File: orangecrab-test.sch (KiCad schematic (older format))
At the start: 27 parts, among them J1 Conn_01x16, J2 Conn_01x12, SW1 SW_Push, U1 DAC53608RTET, U2 MCP23S08T-E-ML

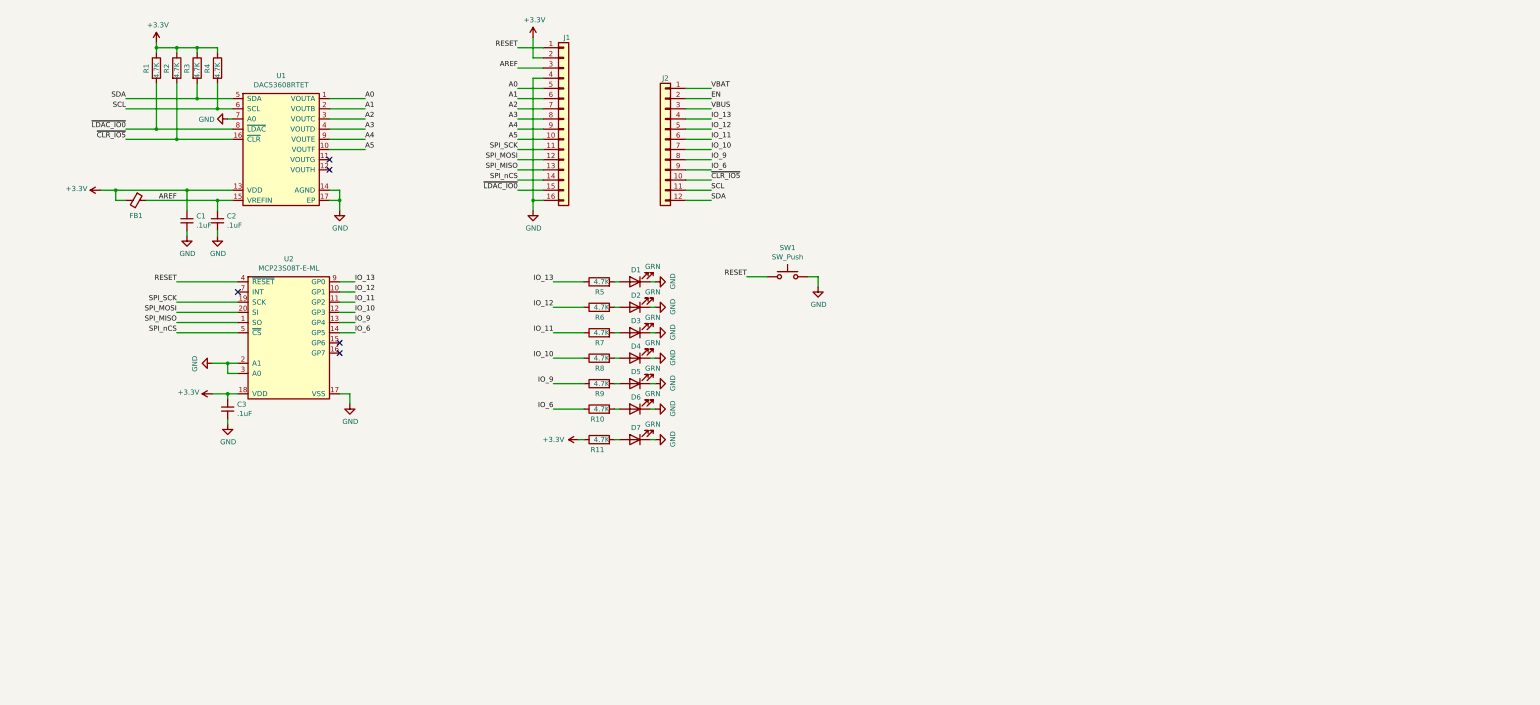
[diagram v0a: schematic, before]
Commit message: Add FTDI from programming the initial firmware
Signed-off-by: Michael Welling <mwelling@ieee.org>
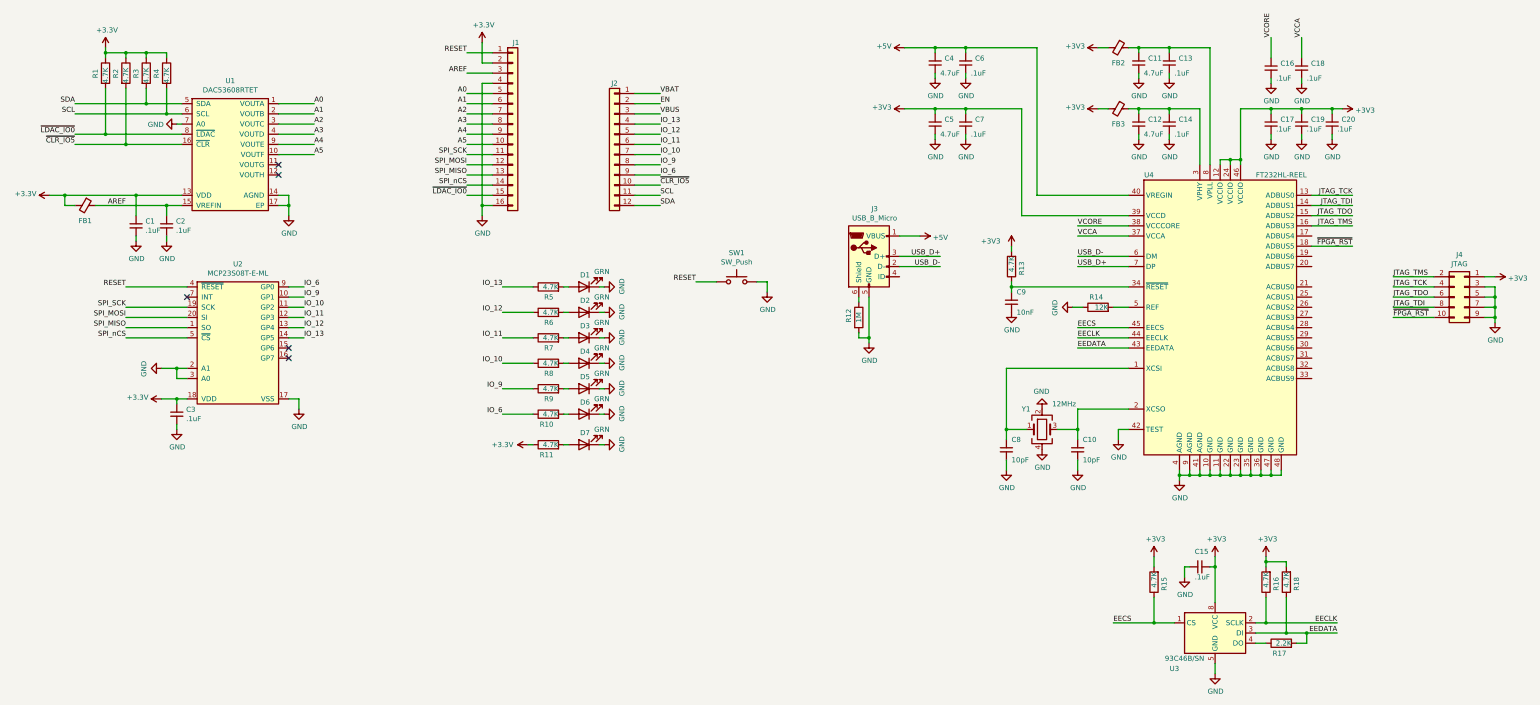
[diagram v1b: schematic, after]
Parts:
- added C10, C8: 10pF, Capacitor_SMD:C_0402_1005Metric, symbol Device:C_Small
- added C11, C12: 4.7uF, Capacitor_SMD:C_0603_1608Metric, symbol Device:C_Small
- added C13, C14, C15, C16, C17, C18, C19, C20, C6, C7: .1uF, Capacitor_SMD:C_0402_1005Metric, symbol Device:C_Small
- added C4, C5: 4.7uF, Capacitor_SMD:C_0402_1005Metric, symbol Device:C_Small
- added C9: 10nF, Capacitor_SMD:C_0402_1005Metric, symbol Device:C_Small
- added FB2, FB3: Ferrite_Bead_Small, Inductor_SMD:L_0603_1608Metric, symbol Device:Ferrite_Bead_Small
- added J3: USB_B_Micro, Connector_USB:USB_Micro-B_Molex-105017-0001, symbol Connector:USB_B_Micro
- added J4: JTAG, Connector_PinHeader_1.27mm:PinHeader_2x05_P1.27mm_Vertical_SMD, symbol Connector_Generic:Conn_02x05_Odd_Even
- added R12: 1M, Resistor_SMD:R_0402_1005Metric, symbol Device:R
- added R13, R15, R16, R18: 4.7K, Resistor_SMD:R_0402_1005Metric, symbol Device:R
- added R14: 12K, Resistor_SMD:R_0402_1005Metric, symbol Device:R
- added R17: 2.2K, Resistor_SMD:R_0402_1005Metric, symbol Device:R
- added U3: 93C46B/SN, Package_SO:SOIC-8_3.9x4.9mm_P1.27mm, symbol Memory_EEPROM:93CxxB
- added U4: FT232HL-REEL, Package_QFP:TQFP-48-1EP_7x7mm_P0.5mm_EP5x5mm, symbol Interface_USB:FT232H
- added Y1: 12MHz, Crystal:Crystal_SMD_2520-4Pin_2.5x2.0mm, symbol Device:Crystal_GND24
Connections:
- net +3V3: now also C15.1, C17.1, C19.1, C20.1, C5.1, C7.1, FB2.2, FB3.2, J4.1 (Pin_1), R13.2, R15.2, R16.2, R18.2, U3.8 (VCC), U4.12 (VCCIO), U4.24 (VCCIO), U4.39 (VCCD), U4.46 (VCCIO)
- net GND: now also C10.2, C11.2, C12.2, C13.2, C14.2, C15.2, C16.2, C17.2, C18.2, C19.2, C20.2, C4.2, C5.2, C6.2, C7.2, C8.2, C9.2, J3.5 (GND), J4.3 (Pin_3), J4.5 (Pin_5), J4.7 (Pin_7), J4.9 (Pin_9), R12.2, R14.1, U3.5 (GND), U4.10 (GND), U4.11 (GND), U4.22 (GND), U4.23 (GND), U4.35 (GND), U4.36 (GND), U4.4 (AGND), U4.41 (AGND), U4.42 (TEST), U4.47 (GND), U4.48 (GND), U4.9 (AGND), Y1.2, Y1.4
- net IO_10: now also U2.11 (GP2); no longer U2.12 (GP3)
- net IO_11: now also U2.12 (GP3); no longer U2.11 (GP2)
- net IO_12: now also U2.13 (GP4); no longer U2.10 (GP1)
- net IO_13: now also U2.14 (GP5); no longer U2.9 (GP0)
- net IO_6: now also U2.9 (GP0); no longer U2.14 (GP5)
- net IO_9: now also U2.10 (GP1); no longer U2.13 (GP4)
- new net: C8.1, U4.1 (XCSI), Y1.1
- new net: C10.1, U4.2 (XCSO), Y1.3
- new net: C12.1, C14.1, FB3.1, U4.3 (VPHY)
- new net: C9.1, R13.1, U4.34 (~RESET)
- new net: R14.2, U4.5 (REF)
- new net: C11.1, C13.1, FB2.1, U4.8 (VPLL)
- new net: R17.1, U3.4 (DO)
- new net: J3.6 (Shield), R12.1
- new net +5V: C4.1, C6.1, J3.1 (VBUS), U4.40 (VREGIN)
- new net EECLK: R16.1, U3.2 (SCLK), U4.44 (EECLK)
- new net EECS: R15.1, U3.1 (CS), U4.45 (EECS)
- new net EEDATA: R17.2, R18.1, U3.3 (DI), U4.43 (EEDATA)
- new net JTAG_TCK: J4.4 (Pin_4), U4.13 (ADBUS0)
- new net JTAG_TDI: J4.8 (Pin_8), U4.14 (ADBUS1)
- new net JTAG_TDO: J4.6 (Pin_6), U4.15 (ADBUS2)
- new net JTAG_TMS: J4.2 (Pin_2), U4.16 (ADBUS3)
- new net USB_D+: J3.3 (D+), U4.7 (DP)
- new net USB_D-: J3.2 (D-), U4.6 (DM)
- new net VCCA: C18.1, U4.37 (VCCA)
- new net VCORE: C16.1, U4.38 (VCCCORE)
- new net ~FPGA_RST: J4.10 (Pin_10), U4.18 (ADBUS5)
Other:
- moved on the sheet: C1, C2, C3, D1, D2, D3, D4, D5, D6, D7, FB1, J1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

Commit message: Route board
Consider making the FTDI a snap off section.

Signed-off-by: Michael Welling <mwelling@ieee.org>
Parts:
- added H1, H2, H3, H4: MountingHole, MountingHole:MountingHole_3.5mm, symbol Mechanical:MountingHole
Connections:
- net +3V3: no longer C15.1, C17.1, C19.1, C20.1, C5.1, C7.1, FB2.2, FB3.2, J4.1 (Pin_1), R13.2, R15.2, R16.2, R18.2, U3.8 (VCC), U4.12 (VCCIO), U4.24 (VCCIO), U4.39 (VCCD), U4.46 (VCCIO)
- new net: C15.1, U3.8 (VCC)
- new net +3.3VA: C17.1, C19.1, C20.1, C5.1, C7.1, FB2.2, FB3.2, R13.2, R15.2, R16.2, R18.2, U4.12 (VCCIO), U4.24 (VCCIO), U4.39 (VCCD), U4.46 (VCCIO)
- no-connect marks 5 -> 6
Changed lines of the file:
@@
 	11400 4150 11500 4150
-$Comp
-L power:+3V3 #PWR0132
-U 1 1 5EC7E2DC
-P 10800 3550
-F 0 "#PWR0132" H 10800 3400 50  0001 C CNN
-F 1 "+3V3" H 10500 3600 50  0000 L CNN
-F 2 "" H 10800 3550 50  0001 C CNN
-F 3 "" H 10800 3550 50  0001 C CNN
-	1    10800 3550
-	1    0    0    -1
-$EndComp
 $Comp
 L Device:R R13
@@
 	13050 2200 13050 2700
 Connection ~ 13050 2700
-$Comp
-L power:+3V3 #PWR0140
-U 1 1 5ED4604E
-P 11650 1600
-F 0 "#PWR0140" H 11650 1450 50  0001 C CNN
-F 1 "+3V3" V 11665 1728 50  0000 L CNN
-F 2 "" H 11650 1600 50  0001 C CNN
-F 3 "" H 11650 1600 50  0001 C CNN
-	1    11650 1600
-	0    -1   -1   0
-$EndComp
-$Comp
-L power:+3V3 #PWR0141
-U 1 1 5ED462A2
-P 11650 2200
-F 0 "#PWR0141" H 11650 2050 50  0001 C CNN
-F 1 "+3V3" V 11665 2328 50  0000 L CNN
-F 2 "" H 11650 2200 50  0001 C CNN
-F 3 "" H 11650 2200 50  0001 C CNN
-	1    11650 2200
-	0    -1   -1   0
-$EndComp
 Wire Wire Line
 	11650 1600 11750 1600
 Wire Wire Line
 	11650 2200 11750 2200
-$Comp
-L power:+3V3 #PWR0142
-U 1 1 5ED5C01E
-P 14050 2200
-F 0 "#PWR0142" H 14050 2050 50  0001 C CNN
-F 1 "+3V3" V 14065 2328 50  0000 L CNN
-F 2 "" H 14050 2200 50  0001 C CNN
-F 3 "" H 14050 2200 50  0001 C CNN
-	1    14050 2200
-	0    1    1    0
-$EndComp
 Wire Wire Line
 	13950 2200 14050 2200
@@
 Wire Wire Line
 	10350 2200 10050 2200
-$Comp
-L power:+3V3 #PWR0148
-U 1 1 5EDF2C7E
-P 9750 2200
-F 0 "#PWR0148" H 9750 2050 50  0001 C CNN
-F 1 "+3V3" V 9765 2328 50  0000 L CNN
-F 2 "" H 9750 2200 50  0001 C CNN
-F 3 "" H 9750 2200 50  0001 C CNN
-	1    9750 2200
-	0    -1   -1   0
-$EndComp
 Wire Wire Line
 	9750 2200 10050 2200
@@
 Wire Wire Line
 	12800 6700 12750 6700
-$Comp
-L power:+3V3 #PWR0153
-U 1 1 5EF89E05
-P 12800 6600
-F 0 "#PWR0153" H 12800 6450 50  0001 C CNN
-F 1 "+3V3" H 12815 6773 50  0000 C CNN
-F 2 "" H 12800 6600 50  0001 C CNN
-F 3 "" H 12800 6600 50  0001 C CNN
-	1    12800 6600
-	1    0    0    -1
-$EndComp
 Wire Wire Line
 	12800 6700 12800 6600
@@
 $EndComp
 $Comp
-L power:+3V3 #PWR0154
-U 1 1 5F163EF8
-P 15550 3850
-F 0 "#PWR0154" H 15550 3700 50  0001 C CNN
-F 1 "+3V3" V 15565 3978 50  0000 L CNN
-F 2 "" H 15550 3850 50  0001 C CNN
-F 3 "" H 15550 3850 50  0001 C CNN
-	1    15550 3850
-	0    1    1    0
-$EndComp
-Wire Wire Line
-	15450 3850 15550 3850
-$Comp
 L power:GND #PWR0155
 U 1 1 5F173112
@@
 Wire Wire Line
 	13500 7350 13700 7350
-$Comp
-L power:+3V3 #PWR0156
-U 1 1 5F1D01BE
-P 13300 6600
-F 0 "#PWR0156" H 13300 6450 50  0001 C CNN
-F 1 "+3V3" H 13315 6773 50  0000 C CNN
-F 2 "" H 13300 6600 50  0001 C CNN
-F 3 "" H 13300 6600 50  0001 C CNN
-	1    13300 6600
-	1    0    0    -1
-$EndComp
 Wire Wire Line
 	13300 6700 13300 6650
@@
 Wire Wire Line
 	12200 7000 12200 7250
-$Comp
-L power:+3V3 #PWR0157
-U 1 1 5F22302D
-P 12200 6600
-F 0 "#PWR0157" H 12200 6450 50  0001 C CNN
-F 1 "+3V3" H 12215 6773 50  0000 C CNN
-F 2 "" H 12200 6600 50  0001 C CNN
-F 3 "" H 12200 6600 50  0001 C CNN
-	1    12200 6600
-	1    0    0    -1
-$EndComp
 Wire Wire Line
 	12800 6700 12800 7050
-Wire Wire Line
-	12200 6700 12200 6600
 Connection ~ 12200 7250
 Wire Wire Line
@@
 Text Label 14150 3550 2    50   ~ 0
 ~FPGA_RST
+$Comp
+L Mechanical:MountingHole H4
+U 1 1 5EB87D65
+P 13450 8900
+F 0 "H4" H 13550 8946 50  0000 L CNN
+F 1 "MountingHole" H 13550 8855 50  0000 L CNN
+F 2 "MountingHole:MountingHole_3.5mm" H 13450 8900 50  0001 C CNN
+F 3 "~" H 13450 8900 50  0001 C CNN
+	1    13450 8900
+	1    0    0    -1
+$EndComp
+$Comp
+L Mechanical:MountingHole H3
+U 1 1 5EB88028
+P 13450 8650
+F 0 "H3" H 13550 8696 50  0000 L CNN
+F 1 "MountingHole" H 13550 8605 50  0000 L CNN
+F 2 "MountingHole:MountingHole_3.5mm" H 13450 8650 50  0001 C CNN
+F 3 "~" H 13450 8650 50  0001 C CNN
+	1    13450 8650
+	1    0    0    -1
+$EndComp
+$Comp
+L Mechanical:MountingHole H2
+U 1 1 5EB99EEE
+P 13450 8400
+F 0 "H2" H 13550 8446 50  0000 L CNN
+F 1 "MountingHole" H 13550 8355 50  0000 L CNN
+F 2 "MountingHole:MountingHole_3.5mm" H 13450 8400 50  0001 C CNN
+F 3 "~" H 13450 8400 50  0001 C CNN
+	1    13450 8400
+	1    0    0    -1
+$EndComp
+$Comp
+L Mechanical:MountingHole H1
+U 1 1 5EBABDBC
+P 13450 8150
+F 0 "H1" H 13550 8196 50  0000 L CNN
+F 1 "MountingHole" H 13550 8105 50  0000 L CNN
+F 2 "MountingHole:MountingHole_3.5mm" H 13450 8150 50  0001 C CNN
+F 3 "~" H 13450 8150 50  0001 C CNN
+	1    13450 8150
+	1    0    0    -1
+$EndComp
+NoConn ~ 15450 3850
+$Comp
+L power:+3.3VA #PWR?
+U 1 1 5EBD0DE3
+P 9750 2200
+F 0 "#PWR?" H 9750 2050 50  0001 C CNN
+F 1 "+3.3VA" V 9765 2327 50  0000 L CNN
+F 2 "" H 9750 2200 50  0001 C CNN
+F 3 "" H 9750 2200 50  0001 C CNN
+	1    9750 2200
+	0    -1   -1   0
+$EndComp
+$Comp
+L power:+3.3VA #PWR?
+U 1 1 5EBD16BF
+P 11650 1600
+F 0 "#PWR?" H 11650 1450 50  0001 C CNN
+F 1 "+3.3VA" V 11665 1727 50  0000 L CNN
+F 2 "" H 11650 1600 50  0001 C CNN
+F 3 "" H 11650 1600 50  0001 C CNN
+	1    11650 1600
+	0    -1   -1   0
+$EndComp
+$Comp
+L power:+3.3VA #PWR?
+U 1 1 5EBD183E
+P 11650 2200
+F 0 "#PWR?" H 11650 2050 50  0001 C CNN
+F 1 "+3.3VA" V 11665 2327 50  0000 L CNN
+F 2 "" H 11650 2200 50  0001 C CNN
+F 3 "" H 11650 2200 50  0001 C CNN
+	1    11650 2200
+	0    -1   -1   0
+$EndComp
+$Comp
+L power:+3.3VA #PWR?
+U 1 1 5EBD197F
+P 14050 2200
+F 0 "#PWR?" H 14050 2050 50  0001 C CNN
+F 1 "+3.3VA" V 14065 2328 50  0000 L CNN
+F 2 "" H 14050 2200 50  0001 C CNN
+F 3 "" H 14050 2200 50  0001 C CNN
+	1    14050 2200
+	0    1    1    0
+$EndComp
+$Comp
+L power:+3.3VA #PWR?
+U 1 1 5EBD1A82
+P 10800 3550
+F 0 "#PWR?" H 10800 3400 50  0001 C CNN
+F 1 "+3.3VA" H 10815 3723 50  0000 C CNN
+F 2 "" H 10800 3550 50  0001 C CNN
+F 3 "" H 10800 3550 50  0001 C CNN
+	1    10800 3550
+	1    0    0    -1
+$EndComp
+$Comp
+L power:+3.3VA #PWR?
+U 1 1 5EBD1C7D
+P 12200 6600
+F 0 "#PWR?" H 12200 6450 50  0001 C CNN
+F 1 "+3.3VA" H 12215 6773 50  0000 C CNN
+F 2 "" H 12200 6600 50  0001 C CNN
+F 3 "" H 12200 6600 50  0001 C CNN
+	1    12200 6600
+	1    0    0    -1
+$EndComp
+Wire Wire Line
+	12200 6600 12200 6700
+$Comp
+L power:+3.3VA #PWR?
+U 1 1 5EBE3E73
+P 13300 6600
+F 0 "#PWR?" H 13300 6450 50  0001 C CNN
+F 1 "+3.3VA" H 13315 6773 50  0000 C CNN
+F 2 "" H 13300 6600 50  0001 C CNN
+F 3 "" H 13300 6600 50  0001 C CNN
+	1    13300 6600
+	1    0    0    -1
+$EndComp
 $EndSCHEMATC

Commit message: Add a few more mounting holes
Signed-off-by: Michael Welling <mwelling@ieee.org>
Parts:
- added H5, H6, H7, H8: MountingHole, MountingHole:MountingHole_3.5mm, symbol Mechanical:MountingHole
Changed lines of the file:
@@
 NoConn ~ 15450 3850
 $Comp
-L power:+3.3VA #PWR?
+L power:+3.3VA #PWR01
 U 1 1 5EBD0DE3
 P 9750 2200
-F 0 "#PWR?" H 9750 2050 50  0001 C CNN
+F 0 "#PWR01" H 9750 2050 50  0001 C CNN
 F 1 "+3.3VA" V 9765 2327 50  0000 L CNN
 F 2 "" H 9750 2200 50  0001 C CNN
@@
 $EndComp
 $Comp
-L power:+3.3VA #PWR?
+L power:+3.3VA #PWR03
 U 1 1 5EBD16BF
 P 11650 1600
-F 0 "#PWR?" H 11650 1450 50  0001 C CNN
+F 0 "#PWR03" H 11650 1450 50  0001 C CNN
 F 1 "+3.3VA" V 11665 1727 50  0000 L CNN
 F 2 "" H 11650 1600 50  0001 C CNN
@@
 $EndComp
 $Comp
-L power:+3.3VA #PWR?
+L power:+3.3VA #PWR04
 U 1 1 5EBD183E
 P 11650 2200
-F 0 "#PWR?" H 11650 2050 50  0001 C CNN
+F 0 "#PWR04" H 11650 2050 50  0001 C CNN
 F 1 "+3.3VA" V 11665 2327 50  0000 L CNN
 F 2 "" H 11650 2200 50  0001 C CNN
@@
 $EndComp
 $Comp
-L power:+3.3VA #PWR?
+L power:+3.3VA #PWR07
 U 1 1 5EBD197F
 P 14050 2200
-F 0 "#PWR?" H 14050 2050 50  0001 C CNN
+F 0 "#PWR07" H 14050 2050 50  0001 C CNN
 F 1 "+3.3VA" V 14065 2328 50  0000 L CNN
 F 2 "" H 14050 2200 50  0001 C CNN
@@
 $EndComp
 $Comp
-L power:+3.3VA #PWR?
+L power:+3.3VA #PWR02
 U 1 1 5EBD1A82
 P 10800 3550
-F 0 "#PWR?" H 10800 3400 50  0001 C CNN
+F 0 "#PWR02" H 10800 3400 50  0001 C CNN
 F 1 "+3.3VA" H 10815 3723 50  0000 C CNN
 F 2 "" H 10800 3550 50  0001 C CNN
@@
 $EndComp
 $Comp
-L power:+3.3VA #PWR?
+L power:+3.3VA #PWR05
 U 1 1 5EBD1C7D
 P 12200 6600
-F 0 "#PWR?" H 12200 6450 50  0001 C CNN
+F 0 "#PWR05" H 12200 6450 50  0001 C CNN
 F 1 "+3.3VA" H 12215 6773 50  0000 C CNN
 F 2 "" H 12200 6600 50  0001 C CNN
@@
 	12200 6600 12200 6700
 $Comp
-L power:+3.3VA #PWR?
+L power:+3.3VA #PWR06
 U 1 1 5EBE3E73
 P 13300 6600
-F 0 "#PWR?" H 13300 6450 50  0001 C CNN
+F 0 "#PWR06" H 13300 6450 50  0001 C CNN
 F 1 "+3.3VA" H 13315 6773 50  0000 C CNN
 F 2 "" H 13300 6600 50  0001 C CNN
@@
 	1    0    0    -1
 $EndComp
+$Comp
+L Mechanical:MountingHole H6
+U 1 1 5EB8A3E3
+P 14250 8400
+F 0 "H6" H 14350 8446 50  0000 L CNN
+F 1 "MountingHole" H 14350 8355 50  0000 L CNN
+F 2 "MountingHole:MountingHole_3.5mm" H 14250 8400 50  0001 C CNN
+F 3 "~" H 14250 8400 50  0001 C CNN
+	1    14250 8400
+	1    0    0    -1
+$EndComp
+$Comp
+L Mechanical:MountingHole H5
+U 1 1 5EB8A3EA
+P 14250 8150
+F 0 "H5" H 14350 8196 50  0000 L CNN
+F 1 "MountingHole" H 14350 8105 50  0000 L CNN
+F 2 "MountingHole:MountingHole_3.5mm" H 14250 8150 50  0001 C CNN
+F 3 "~" H 14250 8150 50  0001 C CNN
+	1    14250 8150
+	1    0    0    -1
+$EndComp
+$Comp
+L Mechanical:MountingHole H8
+U 1 1 5EBAE63F
+P 14250 8900
+F 0 "H8" H 14350 8946 50  0000 L CNN
+F 1 "MountingHole" H 14350 8855 50  0000 L CNN
+F 2 "MountingHole:MountingHole_3.5mm" H 14250 8900 50  0001 C CNN
+F 3 "~" H 14250 8900 50  0001 C CNN
+	1    14250 8900
+	1    0    0    -1
+$EndComp
+$Comp
+L Mechanical:MountingHole H7
+U 1 1 5EBAE646
+P 14250 8650
+F 0 "H7" H 14350 8696 50  0000 L CNN
+F 1 "MountingHole" H 14350 8605 50  0000 L CNN
+F 2 "MountingHole:MountingHole_3.5mm" H 14250 8650 50  0001 C CNN
+F 3 "~" H 14250 8650 50  0001 C CNN
+	1    14250 8650
+	1    0    0    -1
+$EndComp

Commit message: added 2 layers for board/pogo alignment. battery circuit
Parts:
- added C21, C23: 4.7uF, Capacitor_SMD:C_0402_1005Metric, symbol Device:C_Small
- added C22, C24, C?: .1uF, Capacitor_SMD:C_0402_1005Metric, symbol Device:C_Small
- added D8: PMEG3015EH,115, Diode_SMD:D_SOD-123F, symbol Device:D_ALT
- added Q1: DMG2302UK-7, Package_TO_SOT_SMD:SOT-23, symbol Device:Q_NMOS_GSD
- added R19: 402k, Resistor_SMD:R_0402_1005Metric, symbol Device:R
- added R20: 82R, Resistor_SMD:R_1206_3216Metric, symbol Device:R
- added R21: 169k, Resistor_SMD:R_0402_1005Metric, symbol Device:R
- added R22: 4.7K, Resistor_SMD:R_0402_1005Metric, symbol Device:R
- added U5: TPS76301DBVR, Package_TO_SOT_SMD:SOT-23-5, symbol Regulator_Linear:TPS76301
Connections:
- net +5V: now also C?.1, U5.1 (VIN)
- net GND: now also C21.2, C22.2, C23.2, C24.2, C?.2, Q1.2 (S), R21.2, R22.1, U5.2 (GND)
- net VBAT: now also C23.1, C24.1, D8.1 (K), R20.1
- net at U2.15 (GP6): now also U5.3 (EN)
- net at U2.16 (GP7): now also Q1.1 (G), R22.2
- new net: R19.2, R21.1, U5.4 (FB)
- new net: Q1.3 (D), R20.2
- new net 4V: C21.1, C22.1, D8.2 (A), R19.1, U5.5 (VOUT)
- no-connect marks 6 -> 4
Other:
- note added: "1. Test current around 3.3v \npresent across R\ntriggers battery charger"
- note added: "2. Charger passes 100-200mA \ncurrent through Resistor"
- note added: "3. NMOS is required to \n'disconnect' battery"

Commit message: Add regulator input pulldown and add silkscreen bling
Signed-off-by: Michael Welling <mwelling@ieee.org>
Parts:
- removed H7, H8: MountingHole, MountingHole:MountingHole_3.5mm, symbol Mechanical:MountingHole
- added R23: 4.7K, Resistor_SMD:R_0402_1005Metric, symbol Device:R
- gave numbers to parts that had none: 1
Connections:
- net GND: now also R23.1
- net at U2.15 (GP6), U5.3 (EN): now also R23.2
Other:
- moved on the sheet: C1, C2, C3, FB1, R1, R2, R3, R4, U1, U2

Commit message: Add BOM
Signed-off-by: Michael Welling <mwelling@ieee.org>
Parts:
- C1, C13, C14, C15, C16, C17, C18, C19, C2, C20, C22, C24, C25, C3, C6, C7: MPN (none) -> GRM155R71C104KA88J
- C10, C8: MPN (none) -> GRM1555C1H100JA01D
- C11, C12: MPN (none) -> C0603C475K9PACTU
- C21, C23, C4, C5: MPN (none) -> GRM155R60J475ME47D
- C9: MPN (none) -> C0402C103K4RECAUTO
- D1, D2, D3, D4, D5, D6, D7: MPN (none) -> LTST-C191GKT
- D8: MPN (none) -> PMEG3015EH,115
- FB1, FB2, FB3: MPN (none) -> 742792651
- H1, H2, H3, H4, H5, H6, J1, J2: MPN (none) -> N/A
- J3: MPN (none) -> 1050170001
- J4: MPN (none) -> FTSH-105-01-F-DV-K-TR
- Q1: MPN (none) -> DMG2302UK-7
- R1, R10, R11, R13, R15, R16, R18, R2, R22, R23, R3, R4, R5, R6, R7, R8, R9: MPN (none) -> RC0402JR-074K7L
- R12: MPN (none) -> RC0402FR-071ML
- R14: MPN (none) -> ERA-2AEB123X
- R17: MPN (none) -> ERA-2AEB222X
- R19: MPN (none) -> RMCF0402FT402K
- R20: MPN (none) -> RC1206JR-0782RL
- R21: MPN (none) -> RC0402FR-07169KL
- SW1: MPN (none) -> EVQ-P0N02B
- U1: MPN (none) -> DAC53608RTET
- U2: MPN (none) -> MCP23S08T-E-ML
- U3: MPN (none) -> 93C46B/SN
- U4: MPN (none) -> FT232HL-REEL
- U5: MPN (none) -> TPS76301DBVR

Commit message: r0.0 release:  - Design review  - Fixed minor error  - Validate BOM  - Generate and package gerbers for fabrication
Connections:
- net +3.3VA: now also C15.1, U3.8 (VCC)
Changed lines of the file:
@@
 EESchema Schematic File Version 4
-LIBS:orangecrab-test-cache
-EELAYER 26 0
+EELAYER 30 0
 EELAYER END
 $Descr B 17000 11000
 encoding utf-8
 Sheet 1 1
-Title ""
-Date ""
-Rev ""
+Title "OrangeCrab Test Fixture"
+Date "2020-05-16"
+Rev "r0.0"
 Comp ""
-Comment1 ""
-Comment2 ""
+Comment1 "(c) 2020 Michael Welling"
+Comment2 "(c) 2020 Greg Davill"
 Comment3 ""
 Comment4 ""
@@
 Wire Wire Line
 	4000 7150 4000 7200
+$Comp
+L power:+3.3VA #PWR0158
+U 1 1 5EC2B3EF
+P 12800 6600
+F 0 "#PWR0158" H 12800 6450 50  0001 C CNN
+F 1 "+3.3VA" H 12815 6773 50  0000 C CNN
+F 2 "" H 12800 6600 50  0001 C CNN
+F 3 "" H 12800 6600 50  0001 C CNN
+	1    12800 6600
+	1    0    0    -1
+$EndComp
 $EndSCHEMATC
